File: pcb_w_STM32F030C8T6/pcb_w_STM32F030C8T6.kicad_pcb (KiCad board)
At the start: 4 copper layers, 51 x 42 mm, 33 parts, among them J1 Conn_01x04, J2 Conn_01x05, J3 USB_B_Micro, SW1 SW_Push, SW2 SW_SPDT, SW3 SW_Push, SW4 SW_Push, SW5 SW_Push, U1 STM32F030C8Tx, U2 IFX27001TFV33

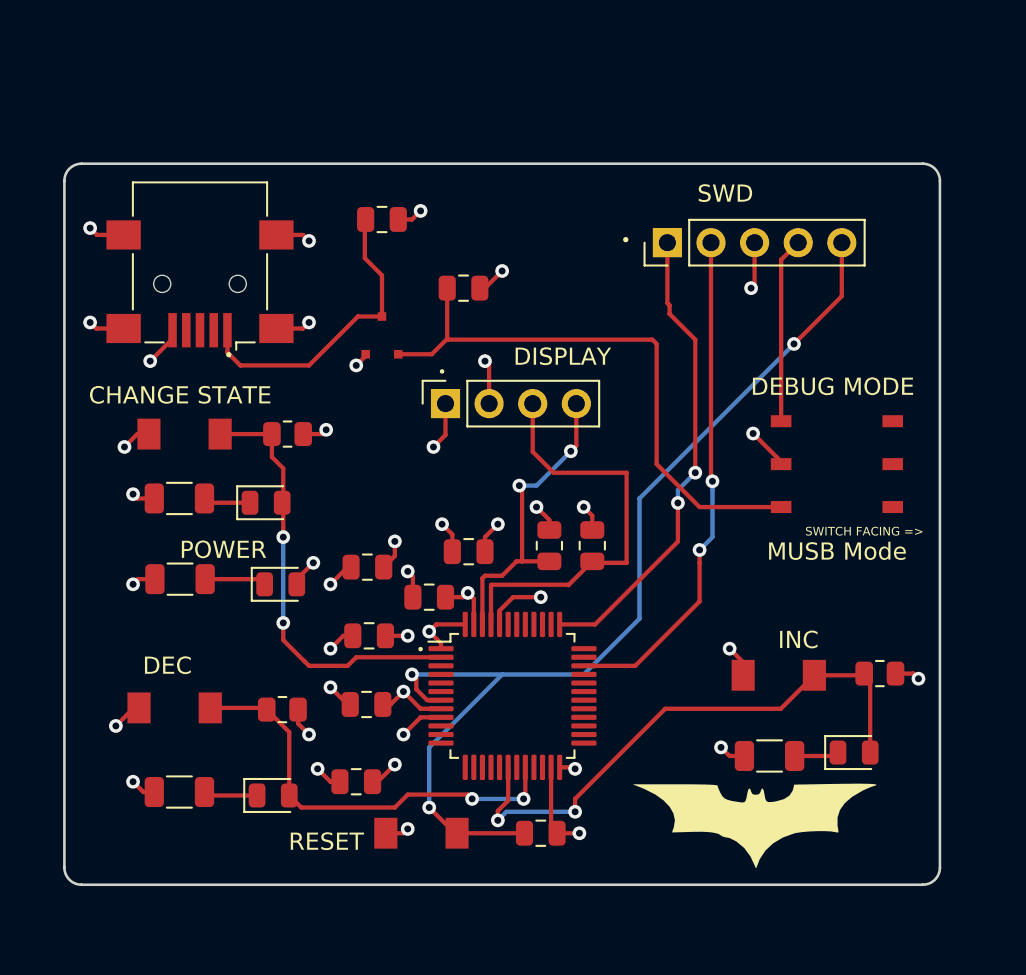
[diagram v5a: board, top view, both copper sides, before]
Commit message: changing components and mc to ones in stock at digikey
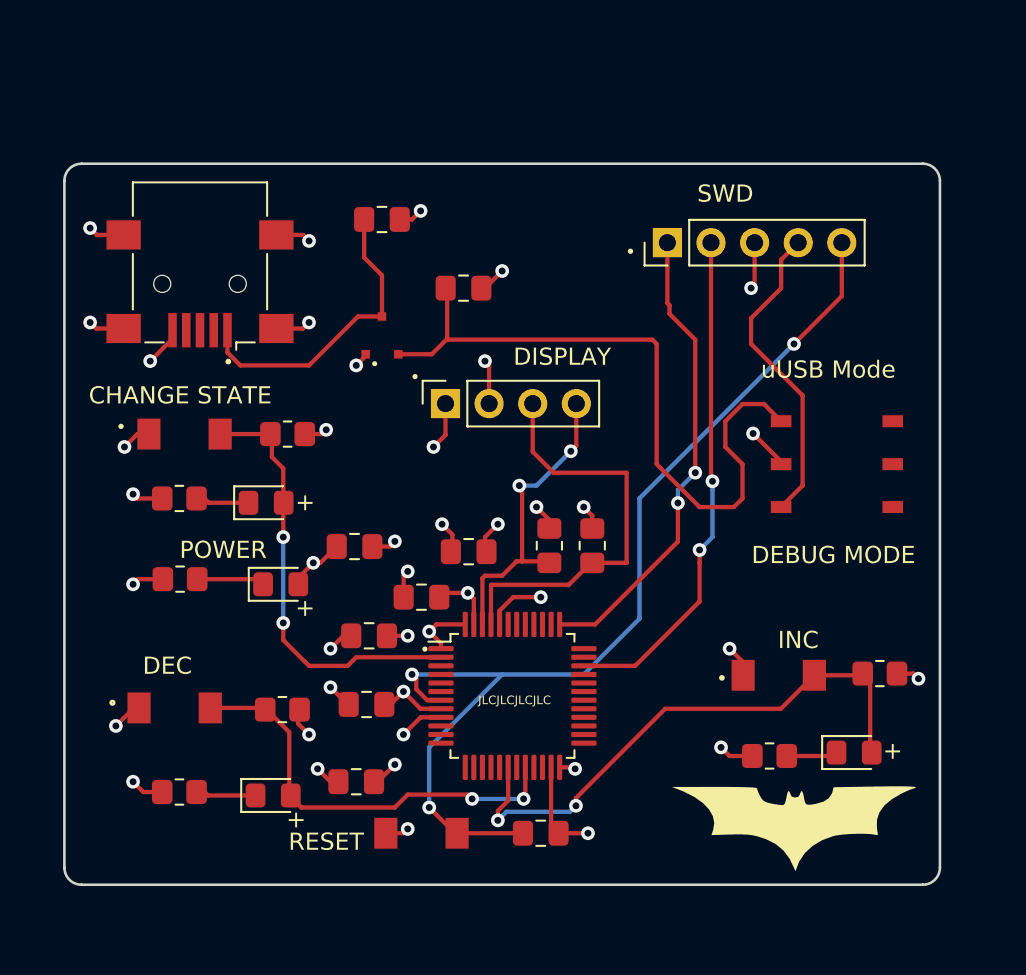
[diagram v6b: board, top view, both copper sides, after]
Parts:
- C1: value 0u1 -> 0.1uF; footprint Capacitor_SMD:C_0805_2012Metric -> Capacitor_SMD:C_0805_2012Metric_Pad1.18x1.45mm_HandSolder
- C2, C3, C4, C5, C6: footprint Capacitor_SMD:C_0805_2012Metric -> Capacitor_SMD:C_0805_2012Metric_Pad1.18x1.45mm_HandSolder
- C7: value 1u -> 1uF; footprint Capacitor_SMD:C_0805_2012Metric -> Capacitor_SMD:C_0805_2012Metric_Pad1.18x1.45mm_HandSolder
- C8, C9: value 1u0 -> 1uF; footprint Capacitor_SMD:C_0805_2012Metric -> Capacitor_SMD:C_0805_2012Metric_Pad1.18x1.45mm_HandSolder
- D1, D2, D3, D4: footprint Diode_SMD:D_0805_2012Metric -> Diode_SMD:D_0805_2012Metric_Pad1.15x1.40mm_HandSolder
- J3: value USB_B_Micro -> USB_B_Mini
- R1, R2, R7, R8, R9: footprint Resistor_SMD:R_0805_2012Metric -> Resistor_SMD:R_0805_2012Metric_Pad1.20x1.40mm_HandSolder
- R3, R4, R5, R6: footprint Resistor_SMD:R_1206_3216Metric -> Resistor_SMD:R_0805_2012Metric_Pad1.20x1.40mm_HandSolder
- moved G*** 2.30 mm to (85.5, 104.7)
- moved C2 1.42 mm to (59.9, 88.3)
- moved C7 0.45 mm to (63.8, 91.2)
- turned SW2 to 0 degrees
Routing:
- net Net-(J2-Pad4): track 10.8 -> 18.3 mm
- net MC_USB_3.3: track 33.8 -> 40.7 mm
- net GND: track 55.1 -> 55.6 mm
- net VDDA: track 32.2 -> 32.3 mm, vias 17 -> 16
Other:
- board text added: "+"
- board text added: "JLCJLCJLCJLC"
- board text added: "uUSB Mode"
- board text removed: "MUSB Mode"
- board text removed: "SWITCH FACING =>"

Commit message: changing linear regulator
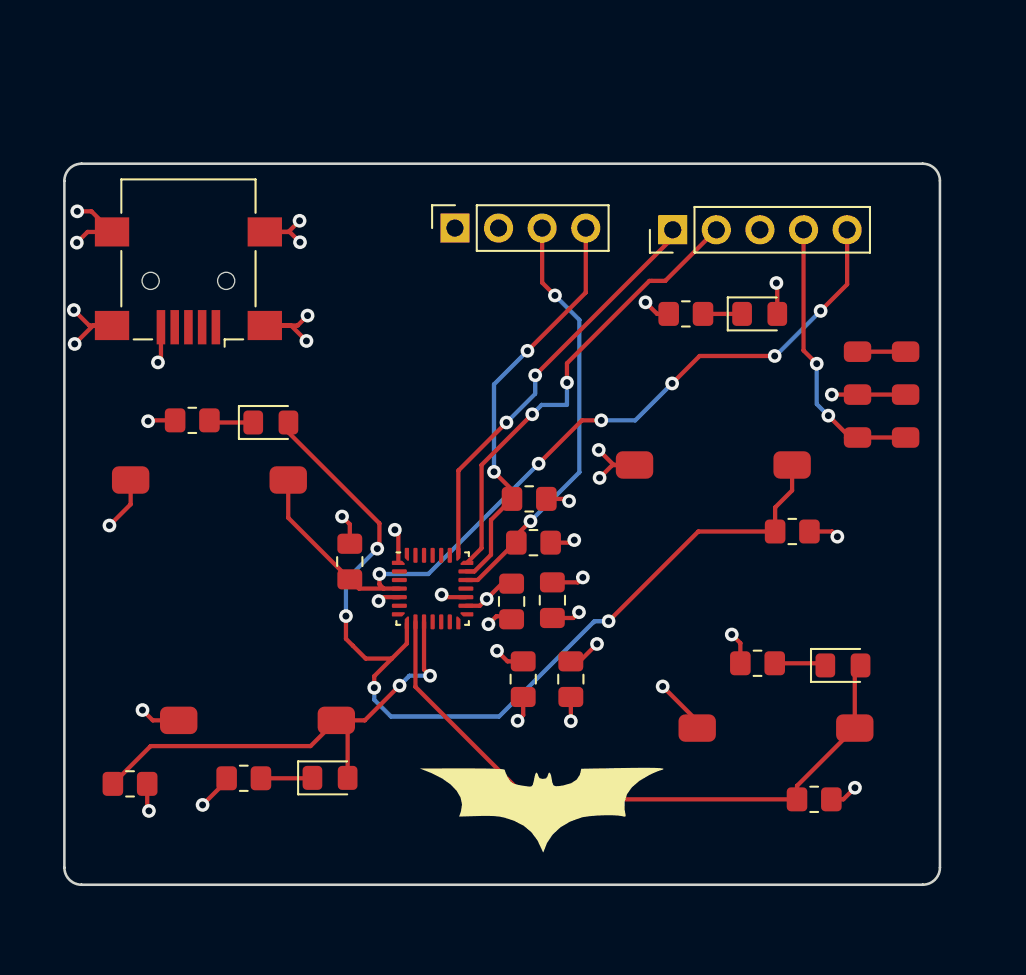
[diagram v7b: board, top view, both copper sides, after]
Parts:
- removed C4, C5: 100n, Capacitor_SMD:C_0805_2012Metric_Pad1.18x1.45mm_HandSolder
- removed C8, C9: 1uF, Capacitor_SMD:C_0805_2012Metric_Pad1.18x1.45mm_HandSolder
- removed U2: IFX27001TFV33, MyLibrary:SOT-23-3L
- SW1, SW3, SW4, SW5: footprint MyLibrary:SMD_3×4×2.0 -> MyLibrary:FSMSMTR-Tactile-Switch-FP
- SW2: footprint MyLibrary:SW-SMD-JLC-C405952 -> MyLibrary:CL-SB-22A-01T-Slide-Switch-FP
- U1: value STM32F030C8Tx -> STM32F031G4Ux; footprint Package_QFP:LQFP-48_7x7mm_P0.5mm -> Package_DFN_QFN:QFN-28_4x4mm_P0.5mm
- moved R3 33.3 mm to (79.2, 74.8)
- moved D1 32.0 mm to (83.5, 74.8)
- moved SW3 30.9 mm to (80.8, 83.5)
- moved R7 29.9 mm to (85.4, 87.4)
- moved SW1 24.0 mm to (51.5, 84.4)
- moved C1 19.3 mm to (59.6, 89.2), turned to 90 degrees
- moved G*** 14.7 mm to (70.8, 103.6)
- moved C2 11.9 mm to (71.4, 91.4), turned to 90 degrees
- moved C3 10.4 mm to (69.0, 91.5), turned to 90 degrees
- moved J1 10.2 mm to (65.8, 69.8)
- moved C7 9.92 mm to (72.5, 96.0), turned to -90 degrees
- moved R9 9.87 mm to (46.8, 102.1)
- moved R8 8.26 mm to (86.7, 103.0)
- moved C6 8.08 mm to (69.7, 96.0), turned to -90 degrees
- moved U1 7.79 mm to (64.5, 90.8)
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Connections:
- R1 pad 1: SCL -> SDA
- R2 pad 1: SDA -> SCL
- U1 pad 1: VDDA -> GND
- U1 pad 10: unconnected-(U1-Pad10) -> DEC
- U1 pad 16: unconnected-(U1-Pad16) -> GND
- U1 pad 17: unconnected-(U1-Pad17) -> VDDA
- U1 pad 18: INC -> unconnected-(U1-Pad18)
- U1 pad 19: unconnected-(U1-Pad19) -> SCL
- U1 pad 2: CHANGE_STATE -> unconnected-(U1-Pad2)
- U1 pad 20: DEC -> SDA
- U1 pad 21: unconnected-(U1-Pad21) -> SWDIO
- U1 pad 22: unconnected-(U1-Pad22) -> SWCLK
- U1 pad 23: GND -> unconnected-(U1-Pad23)
- U1 pad 24: VDDA -> unconnected-(U1-Pad24)
- U1 pad 4: unconnected-(U1-Pad4) -> NRST
- U1 pad 5: unconnected-(U1-Pad5) -> VDDA
- U1 pad 7: NRST -> unconnected-(U1-Pad7)
- U1 pad 8: GND -> CHANGE_STATE
- U1 pad 9: VDDA -> INC
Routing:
- net MC_USB_3.3: track 40.7 -> 3.22 mm
- net CHANGE_STATE: track 25.4 -> 56.5 mm, vias 2 -> 4
- net MC_USB_5: track 17.9 -> 0.00 mm
- net NRST: track 59.7 -> 48.7 mm, vias 3 -> 6
- net SDA: track 18.2 -> 24.1 mm
- net GND: track 55.6 -> 49.9 mm, vias 26 -> 23
- net INC: track 33.2 -> 38.1 mm, vias 2 -> 0
- net SWCLK: track 27.4 -> 24.1 mm
- net VDDA: track 32.3 -> 29.1 mm, vias 16 -> 14
- net DEC: track 25.1 -> 28.0 mm
- net SWDIO: track 29.5 -> 26.8 mm
- net Net-(D1-Pad1): track 3.59 -> 2.27 mm
- net Net-(J2-Pad4): track 18.3 -> 17.1 mm, vias 0 -> 2
- net SCL: track 24.8 -> 24.6 mm, vias 0 -> 2
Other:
- board text removed: "+"
- board text removed: "CHANGE STATE"
- board text removed: "DEBUG MODE"
- board text removed: "DEC"
- board text removed: "DISPLAY"
- board text removed: "INC"
- board text removed: "JLCJLCJLCJLC"
- board text removed: "POWER"
- board text removed: "RESET"
- board text removed: "SWD"
- board text removed: "uUSB Mode"

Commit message: finished schematic fixes and finished pcb
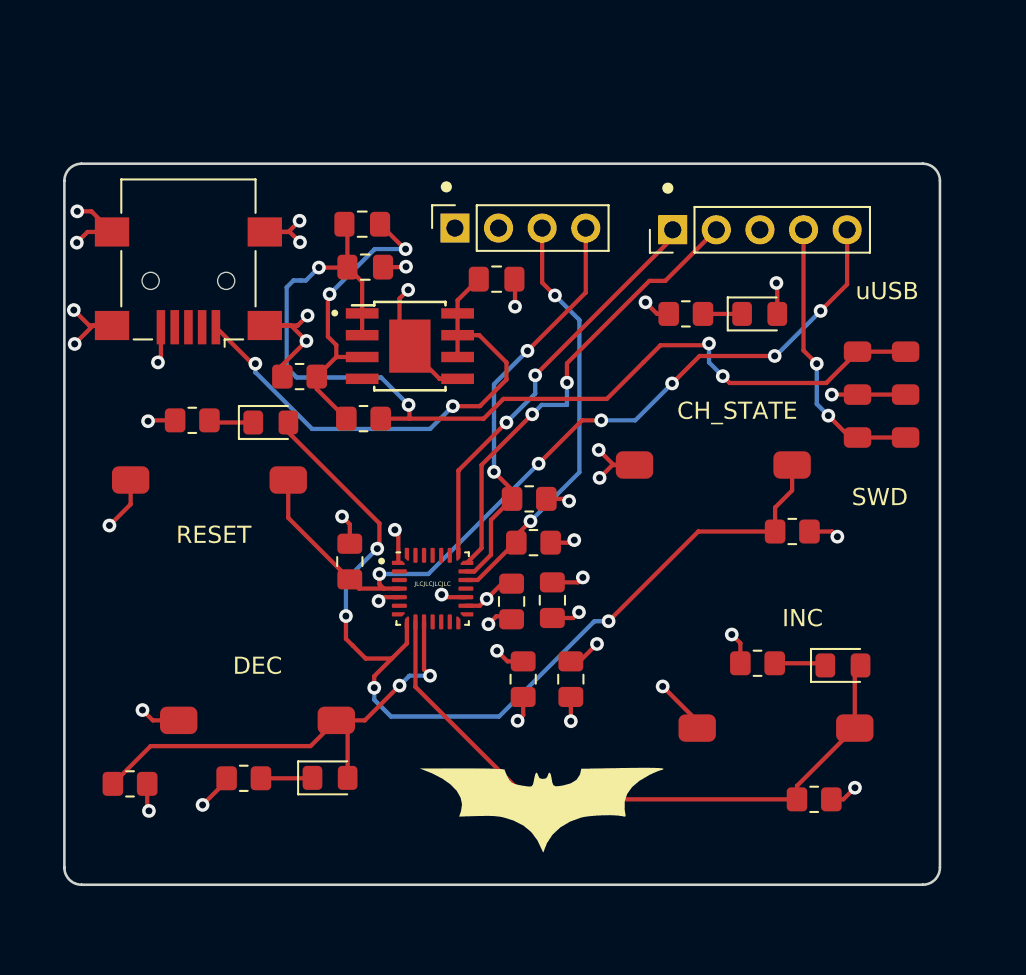
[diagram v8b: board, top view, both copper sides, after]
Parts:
- added C4: 10uF, Capacitor_SMD:C_0805_2012Metric_Pad1.18x1.45mm_HandSolder, F.Cu at (68.2, 72.7)
- added C5: 2700pF, Capacitor_SMD:C_0805_2012Metric_Pad1.18x1.45mm_HandSolder, F.Cu at (60.4, 69.5)
- added C8: 10uF, Capacitor_SMD:C_0805_2012Metric_Pad1.18x1.45mm_HandSolder, F.Cu at (60.5, 72.0)
- added R10: 2k, Resistor_SMD:R_0805_2012Metric_Pad1.20x1.40mm_HandSolder, F.Cu at (60.4, 80.8)
- added R11: 357, Resistor_SMD:R_0805_2012Metric_Pad1.20x1.40mm_HandSolder, F.Cu at (56.7, 78.4)
- added U2: LP38511-ADJ, MyLibrary:TI_SO-PowerPAD-8-GND_DAP, F.Cu at (63.1, 76.6)
- C6: value 10n -> 10nF
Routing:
- net MC_USB_3.3: track 3.22 -> 59.2 mm, vias 0 -> 4
- net MC_USB_5: track 0.00 -> 30.4 mm, vias 0 -> 2
- net Net-(C5-Pad2): track 0.00 -> 17.8 mm, vias 0 -> 2
- net GND: track 49.9 -> 64.8 mm, vias 23 -> 26
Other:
- board text added: "CH_STATE"
- board text added: "DEC"
- board text added: "INC"
- board text added: "JLCJLCJLCJLC"
- board text added: "RESET"
- board text added: "SWD"
- board text added: "uUSB"
